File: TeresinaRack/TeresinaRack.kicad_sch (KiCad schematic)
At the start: 205 parts, among them J3 USB_Micro-B, J4 SWD, J5 PATCH_SM_EDGE, Q1 MMBT3904, Q2 MMBT3904, SW1 RESET, SW2 BOOT, U1 STM32H750IBK6, U12 TL074, U13 MCP6004, U14 MCP6004, U15 MCP6004, U16 LM4040DBZ-10, U2 IS25LP064A, U3 IS42S32160F-6BLI, U4 PCM3060, U6 TPS62170DSGR, U7 LD1117S50, U8 USBLC6-2SC6, Y1 16MHz

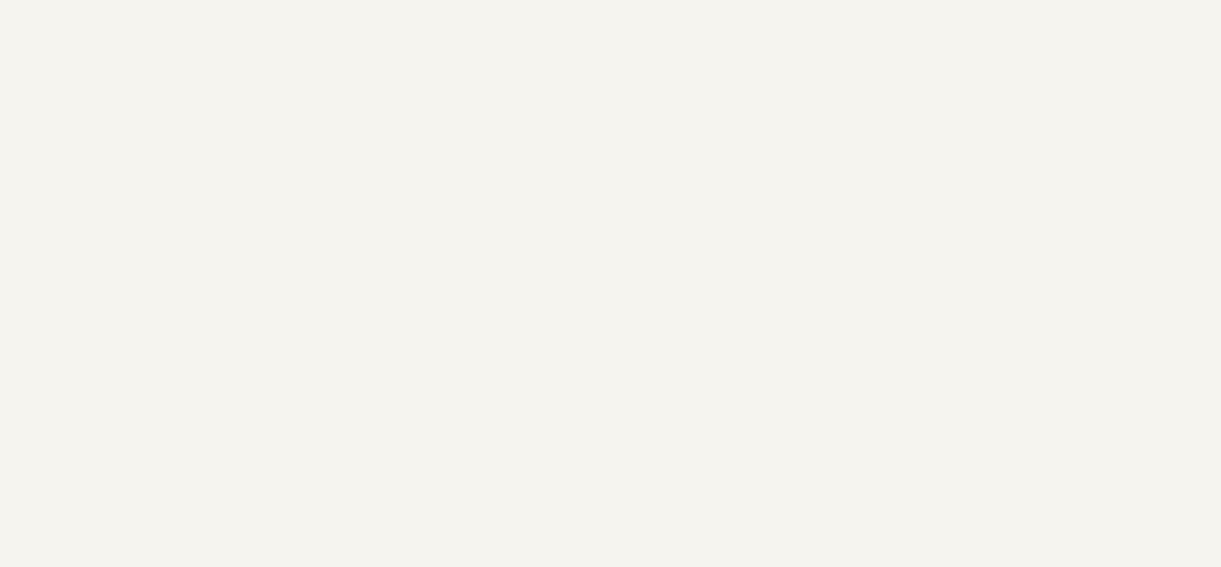
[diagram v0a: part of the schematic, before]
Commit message: Fab-readiness pass: SDRAM decoupling, debris cleanup, doc fixes
- Add C204-C207 (100nF 0402, F.Cu under U3): SDRAM +3V3 ball decoupling
  coverage 4/14 -> 14/14 within 5mm. Verified congruent (sch+pcb+BOM),
  0 existing footprints moved, DRC 0-err/0-unconnected.
- Remove 84 autorouter-debris track stubs + 2 orphan vias (track_dangling
  9 -> 0); connectivity provably intact.
- README: J5 is through-hole pin-header (NOT castellated - do not enable
  castellated holes at order); U1 top / U3 bottom; honest DRC/ERC counts;
  document accepted VCAP-12mm and R201 courtyard margins with evidence;
  part count 208.
- VCAP relocation and R201 nudge assessed and deliberately NOT forced
  (would rip up FMC escape routing; risk > benefit).
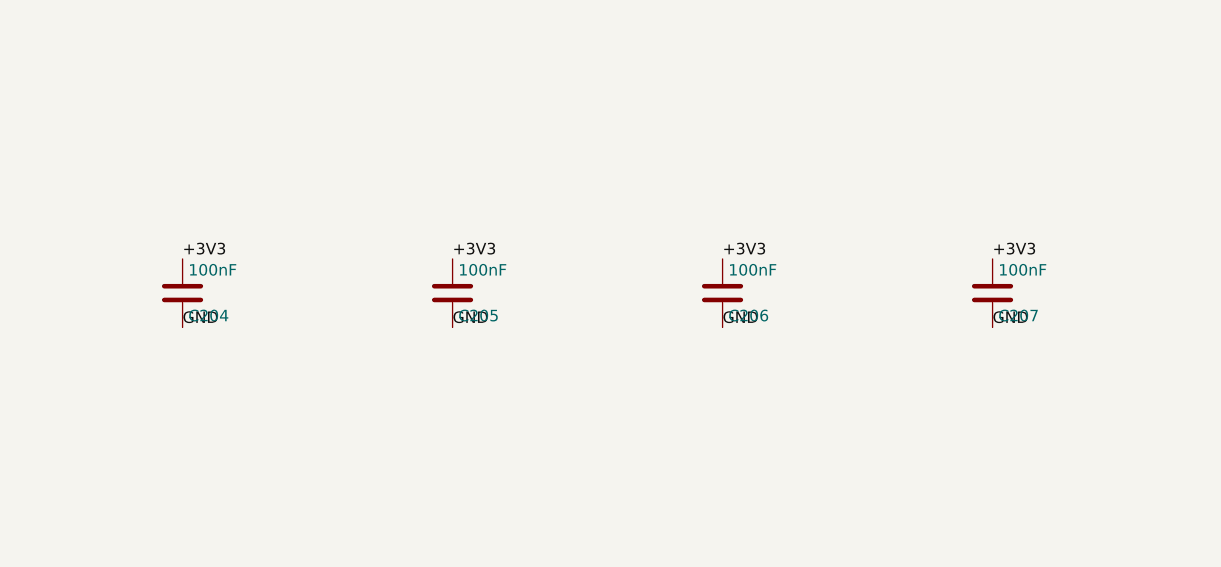
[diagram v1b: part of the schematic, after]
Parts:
- added C204, C205, C206, C207: 100nF, Capacitor_SMD:C_0402_1005Metric, symbol Device:C
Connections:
- net +3V3: now also C204.1, C205.1, C206.1, C207.1
- net GND: now also C204.2, C205.2, C206.2, C207.2

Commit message: Add missing LCSC/MPN on C202/C203/FB9 (codec +5VA filter)
These 3 parts (added with the +5VA codec-supply fix) had LCSC/MPN on
the PCB footprint but NOT on the schematic symbol, so the schematic-
generated BOM omitted them - they would have been left unpopulated at
assembly. Set on the symbol to match the footprint:
  C202 100nF -> C1525, C203 10uF -> C15850, FB9 600R ferrite -> C175716.
Full BOM re-audit: all 208 assembly parts now carry a valid LCSC.
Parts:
- C202: LCSC (none) -> C1525; MPN (none) -> CL05B104KO5NNNC
- C203: LCSC (none) -> C15850; MPN (none) -> CL21A106KAYNNNE
- FB9: LCSC (none) -> C175716; MPN (none) -> CR0805FR600P05Z
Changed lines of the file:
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@@
+			)
+		)
+		(property "LCSC" "C175716"
+			(at 0 0 0)
+			(effects
+				(font
+					(size 1.27 1.27)
+				)
+				(hide yes)
+			)
+		)
+		(property "MPN" "CR0805FR600P05Z"
+			(at 0 0 0)
+			(effects
+				(font
+					(size 1.27 1.27)
+				)
+				(hide yes)
 			)
 		)
@@
 			)
 		)
+		(property "LCSC" "C1525"
+			(at 0 0 0)
+			(effects
+				(font
+					(size 1.27 1.27)
+				)
+				(hide yes)
+			)
+		)
+		(property "MPN" "CL05B104KO5NNNC"
+			(at 0 0 0)
+			(effects
+				(font
+					(size 1.27 1.27)
+				)
+				(hide yes)
+			)
+		)
 		(pin "1"
 		)
@@
 			)
 		)
+		(property "LCSC" "C15850"
+			(at 0 0 0)
+			(effects
+				(font
+					(size 1.27 1.27)
+				)
+				(hide yes)
+			)
+		)
+		(property "MPN" "CL21A106KAYNNNE"
+			(at 0 0 0)
+			(effects
+				(font
+					(size 1.27 1.27)
+				)
+				(hide yes)
+			)
+		)
